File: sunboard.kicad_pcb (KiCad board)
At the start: 2 copper layers, 42.7 x 27.4 mm, 25 parts, among them J1 Conn_01x04, J2 Conn_01x02, J3 Barrel_Jack, J4 Conn_01x04, SW1 SW_Push, U1 STM32F030C8Tx, U4 MIC5209, Y1 Crystal_Small

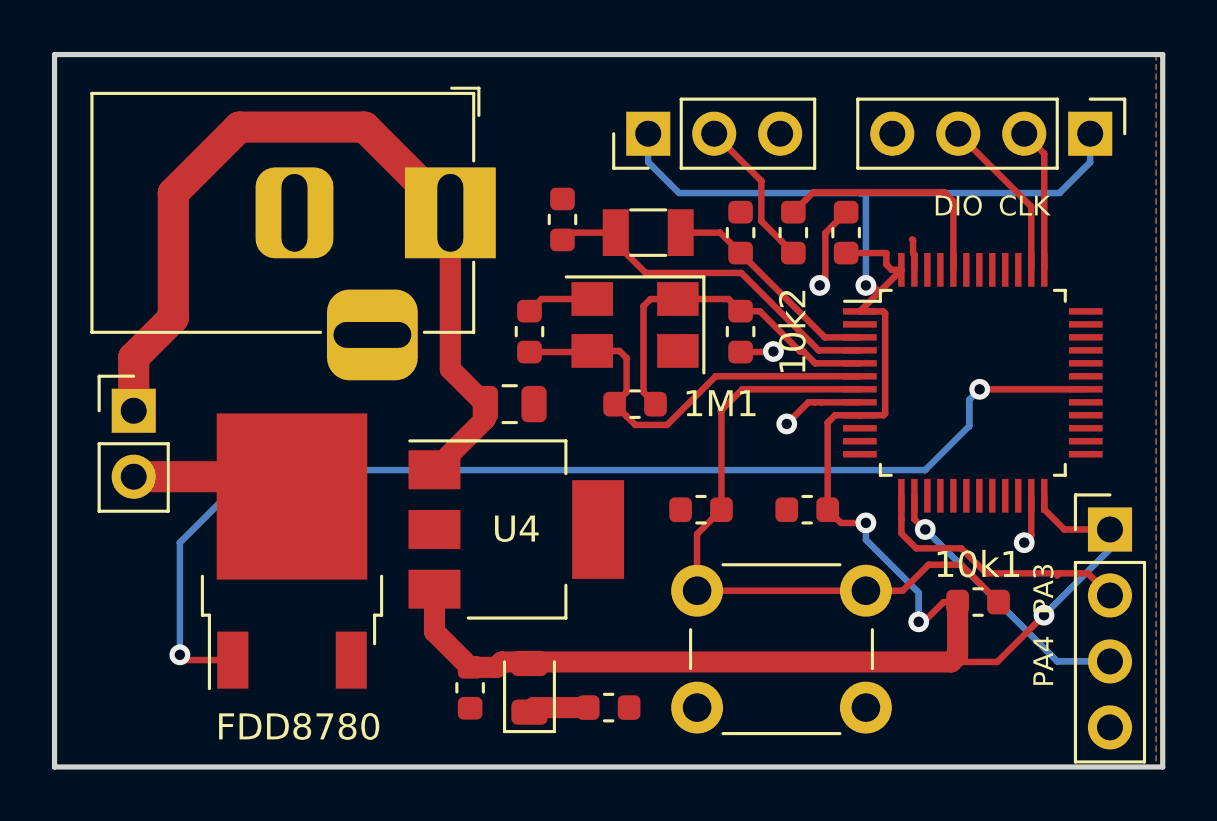
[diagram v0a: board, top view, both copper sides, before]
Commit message: Fixed programming header. Fixed order of header
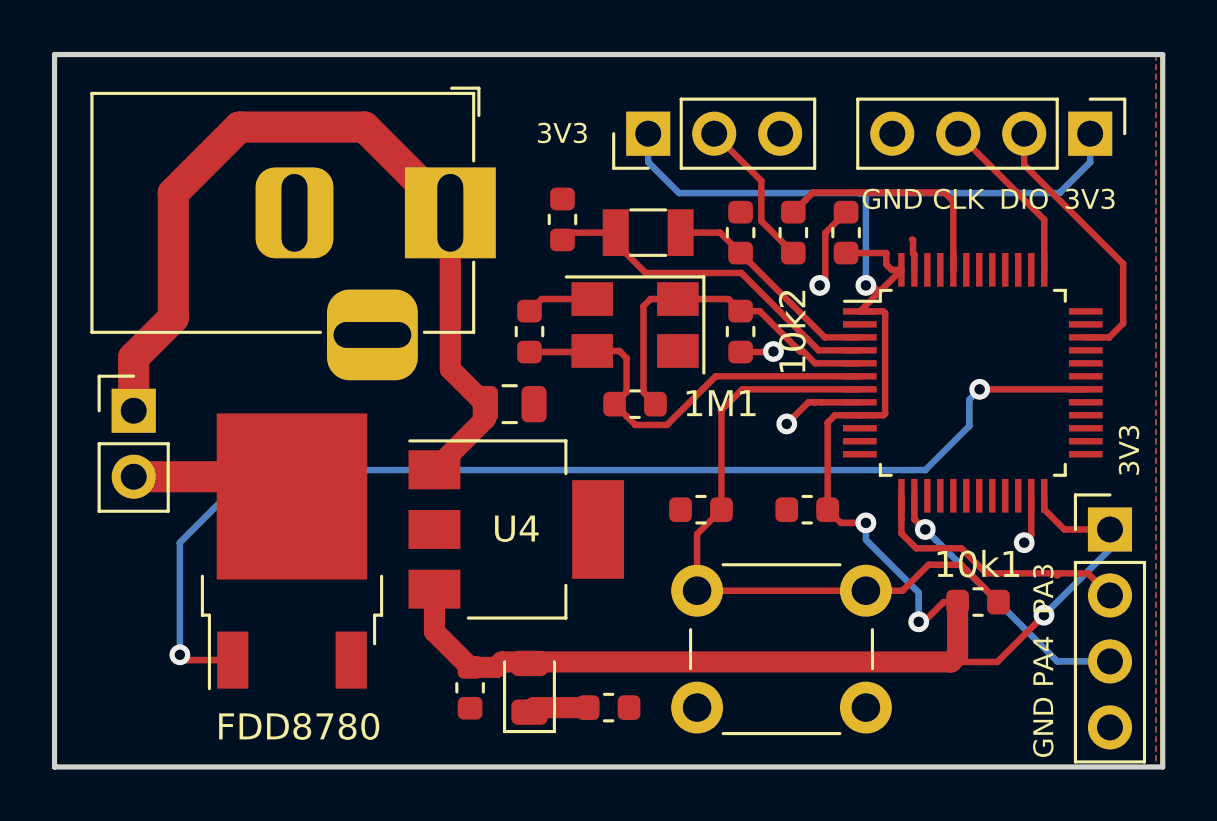
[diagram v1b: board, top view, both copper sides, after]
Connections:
- J1 pad 2: /SWCLK -> /SWDIO
- J1 pad 3: /SWDIO -> /SWCLK
- U1 pad 34: Net-(U1-Pad34) -> /SWDIO
- U1 pad 38: /SWDIO -> Net-(U1-Pad38)
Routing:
- net /SWDIO: track 6.41 -> 10.5 mm
- net /SWCLK: track 5.56 -> 6.61 mm
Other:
- board text added: "3V3"
- board text added: "GND"

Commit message: updated sch and pcb
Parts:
- removed 12pF1, 12pF2: C, Capacitor_SMD:C_0603_1608Metric
- removed 32.768kHz1: Crystal_Small, Crystal:Crystal_SMD_3215-2Pin_3.2x1.5mm
- 0.1uF1, 0.1uF2, 10k1, 1k1, PWR_LED1, U4: moved to B.Cu
- U1: value STM32F030C8Tx -> STM32F030F4Px; footprint Package_QFP:LQFP-48_7x7mm_P0.5mm -> Package_SO:TSSOP-20_4.4x6.5mm_P0.65mm
- moved 0.1uF5 16.7 mm to (82.3, 38.1), turned to 270 degrees
- moved 0.1uF4 14.9 mm to (82.3, 34.0), turned to 270 degrees
- moved 10k1 10.9 mm to (67.1, 41.9)
- moved U4 9.45 mm to (64.0, 35.6)
- moved 1k1 8.96 mm to (60.5, 41.9), turned to 90 degrees
- moved 0.1uF2 7.98 mm to (56.1, 41.9), turned to 90 degrees
- moved PWR_LED1 7.98 mm to (58.4, 41.9), turned to 270 degrees
- moved SW1 6.75 mm to (70.4, 44.2)
- moved FDD8780 3.28 mm to (52.8, 42.2), turned to 180 degrees
- moved U1 2.08 mm to (77.0, 36.0), turned to 90 degrees
- moved 1M1 2.05 mm to (64.0, 36.8)
- moved Y1 2.05 mm to (64.0, 33.8)
- moved 20pF1 2.05 mm to (68.1, 34.0)
- moved 20pF2 2.05 mm to (59.9, 34.0)
- moved 0.1uF1 1.83 mm to (57.4, 37.8), turned to 270 degrees
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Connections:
- U1 pad 1: +3V3 -> /BOOT0
- U1 pad 10: Net-(U1-Pad10) -> /PA4
- U1 pad 13: /PA3 -> Net-(U1-Pad13)
- U1 pad 14: /PA4 -> Net-(U1-Pad14)
- U1 pad 15: Net-(U1-Pad15) -> GND
- U1 pad 16: Net-(U1-Pad16) -> +3V3
- U1 pad 17: Net-(U1-Pad17) -> /PWM
- U1 pad 19: Net-(U1-Pad19) -> /SWDIO
- U1 pad 2: Net-(U1-Pad2) -> Net-(1M1-Pad1)
- U1 pad 20: Net-(U1-Pad20) -> /SWCLK
- U1 pad 3: Net-(12pF1-Pad1) -> Net-(1M1-Pad2)
- U1 pad 4: Net-(12pF2-Pad1) -> /RESET
- U1 pad 5: Net-(1M1-Pad1) -> +3V3
- U1 pad 6: Net-(1M1-Pad2) -> Net-(U1-Pad6)
- U1 pad 7: /RESET -> Net-(U1-Pad7)
- U1 pad 8: GND -> Net-(U1-Pad8)
- U1 pad 9: +3V3 -> /PA3
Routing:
- net +3V3: track 84.9 -> 0.76 mm, vias 4 -> 0
- net /PWM: track 44.4 -> 0.00 mm, vias 2 -> 0
- net /RESET: track 25.6 -> 0.00 mm
- net Net-(12pF2-Pad1): track 13.7 -> 0.00 mm
- net +12V: track 33.4 -> 22.1 mm
- net /PA4: track 10.7 -> 0.00 mm, vias 1 -> 0
- net /PA3: track 10.6 -> 0.00 mm
- net Net-(1M1-Pad2): track 16.4 -> 5.83 mm
- net /SWDIO: track 10.5 -> 0.00 mm
- net GND: track 13.4 -> 3.89 mm, vias 4 -> 1
- net /BOOT0: track 9.26 -> 0.00 mm
- net Net-(12pF1-Pad1): track 8.57 -> 0.00 mm
- net /SWCLK: track 6.61 -> 0.00 mm
- net Net-(10k2-Pad1): track 5.86 -> 0.00 mm
- net Net-(1M1-Pad1): track 13.4 -> 8.01 mm
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- removed copper zone on B.Cu, net GND
- removed copper zone on F.Cu, net GND
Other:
- board size 42.7 x 27.4 mm -> 42.7 x 21.1 mm
- board text removed: "Sunboard Controller v1 Feb 2019"
